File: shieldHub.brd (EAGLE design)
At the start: 70 x 70 mm, 11 parts

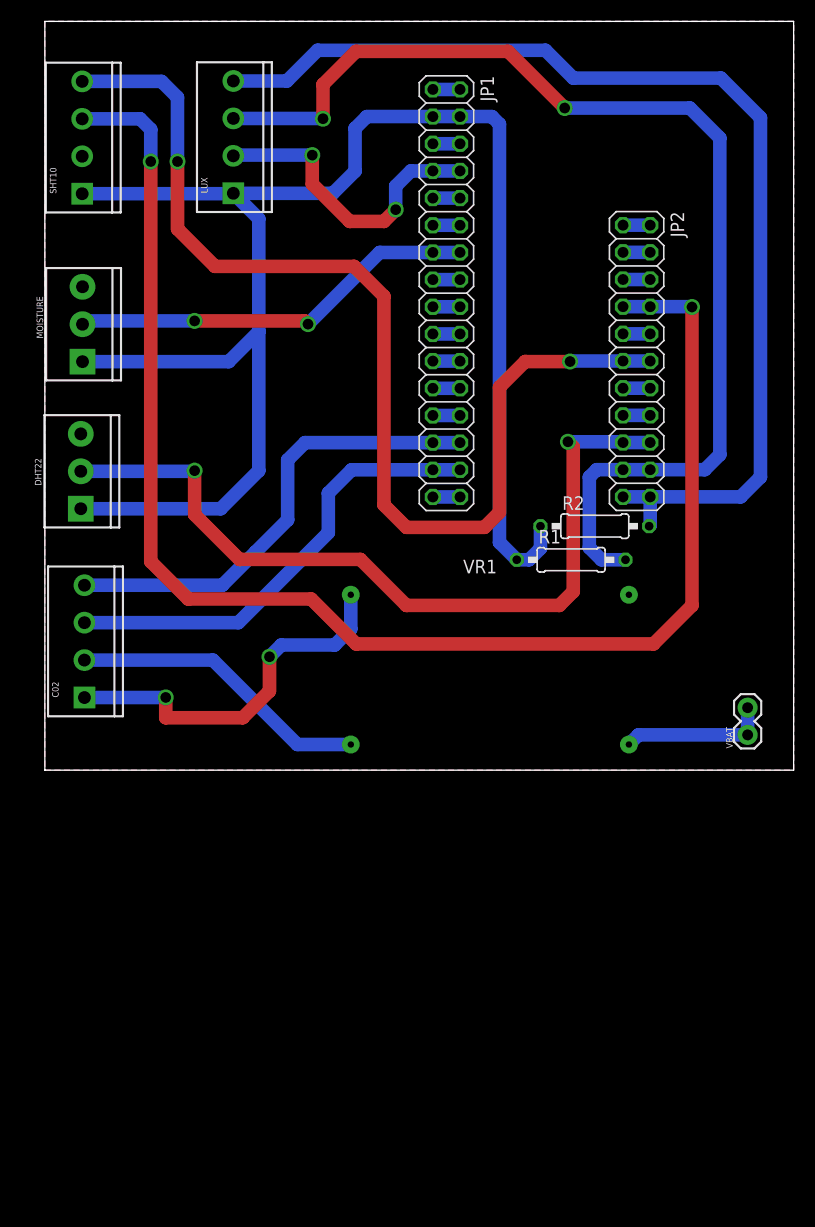
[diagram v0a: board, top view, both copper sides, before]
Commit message: Removes sensor connector pins and adds rrm69 header pin
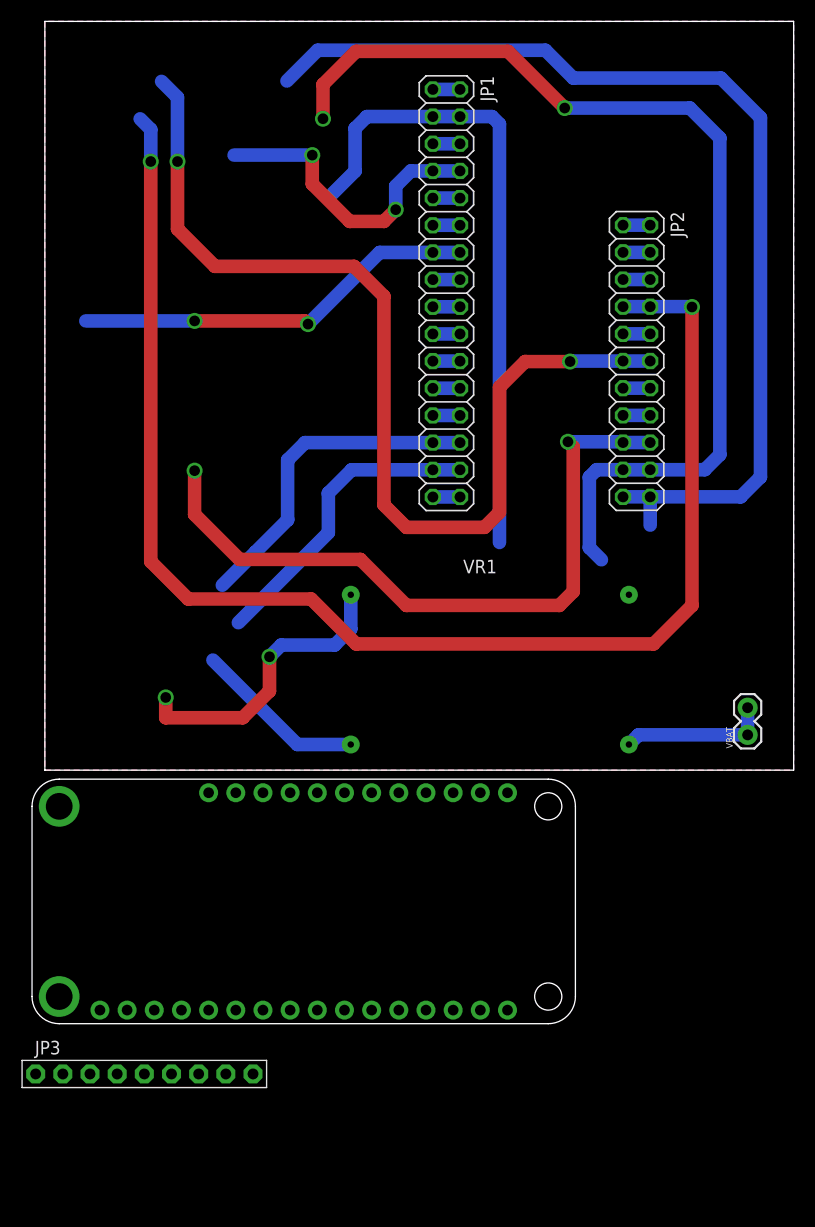
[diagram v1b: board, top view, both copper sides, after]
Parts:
- removed C02, LUX, SHT10: (no value), SparkFun-Connectors:SCREWTERMINAL-3.5MM-4
- removed DHT22, MOISTURE: (no value), SparkFun-Connectors:SCREWTERMINAL-3.5MM-3
- removed R1, R2: 10k, resistor:0207/10
- added JP3: (no value), adafruit:1X09-BIG
- added MS1: FEATHERWING, adafruit:FEATHERWING
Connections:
- net 10_SDA: no longer SHT10.4
- net 12_SCL: no longer SHT10.3
- net 3V: no longer DHT22.1, LUX.1, MOISTURE.1, R1.1, R2.1, SHT10.1
- net 5V: no longer C02.2
- net A2: no longer MOISTURE.2
- net D5: no longer DHT22.2
- net GND: now also MS1.4; no longer C02.1, DHT22.3, LUX.2, MOISTURE.3, SHT10.2
- net RX: no longer C02.4
- net SCL: no longer LUX.3, R1.2
- net SDA: no longer LUX.4, R2.2
- net TX: no longer C02.3
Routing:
- net 3V: track 153.4 -> 60.3 mm
- net TX: track 43.2 -> 28.8 mm
- net RX: track 43.9 -> 31.0 mm
- net 5V: track 28.2 -> 16.2 mm
- net SCL: track 106.4 -> 95.8 mm
- net D5: track 76.2 -> 65.6 mm
- net GND: track 63.9 -> 56.2 mm
- net 10_SDA: track 102.3 -> 94.9 mm
- net 12_SCL: track 136.9 -> 131.4 mm
- net SDA: track 103.1 -> 97.9 mm

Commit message: Adds connector pin for fan power
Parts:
- added VFAN: (no value), SparkFun-Connectors:1X02
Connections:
- removed net 5V: VR1.OUT+
- new net 12V: VFAN.1, VR1.OUT+
- net GND: now also VFAN.2
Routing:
- net 5V: track 16.2 -> 0.00 mm
- net 12V: track 0.00 -> 16.2 mm
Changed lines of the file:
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@@
 <attribute name="VALUE" x="-0.86" y="-31.575" size="1.27" layer="27"/>
+</element>
+<element name="VFAN" library="SparkFun-Connectors" package="1X02" value="" x="-0.4" y="-32.1" smashed="yes">
+<attribute name="NAME" x="-1.67" y="-30.703" size="0.6096" layer="25" font="vector" ratio="20"/>
+<attribute name="VALUE" x="-1.67" y="-34.132" size="0.6096" layer="27" font="vector" ratio="20"/>
 </element>
 </elements>
@@
 <wire x1="21" y1="7.4" x2="18.5" y2="4.9" width="1.27" layer="1"/>
 <contactref element="MS1" pad="4"/>
+<contactref element="VFAN" pad="2"/>
 <wire x1="28.6" y1="16.4" x2="32.8" y2="52.4" width="0" layer="19" extent="1-1"/>
 <wire x1="54.6" y1="16.4" x2="28.6" y2="16.4" width="0" layer="19" extent="1-1"/>
 <wire x1="12.77" y1="-22.43" x2="11.29" y2="6.79" width="0" layer="19" extent="16-16"/>
+<wire x1="2.14" y1="-32.1" x2="12.77" y2="-22.43" width="0" layer="19" extent="1-1"/>
 </signal>
 <signal name="N$1">
@@
 <wire x1="55.5" y1="3.3" x2="65.7" y2="3.3" width="1.27" layer="16"/>
 </signal>
-<signal name="5V">
+<signal name="12V">
 <contactref element="VR1" pad="OUT+"/>
 <wire x1="23.6" y1="2.4" x2="28.6" y2="2.4" width="1.27" layer="16"/>
 <wire x1="15.71" y1="10.29" x2="23.6" y2="2.4" width="1.27" layer="16"/>
+<contactref element="VFAN" pad="1"/>
+<wire x1="28.6" y1="2.4" x2="-0.4" y2="-32.1" width="0" layer="19" extent="1-1"/>
 </signal>
 <signal name="10_SDA">

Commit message: Adds connector for button
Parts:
- added BUTTON: (no value), SparkFun-Connectors:SCREWTERMINAL-3.5MM-2_LOCK
- renumbered JP3 to RFM69
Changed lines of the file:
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@@
 </element>
 <element name="MS1" library="adafruit" package="FEATHERWING" value="FEATHERWING" x="-1.2" y="-23.7" smashed="yes"/>
-<element name="JP3" library="adafruit" package="1X09-BIG" value="" x="9.3" y="-28.4" smashed="yes">
+<element name="RFM69" library="adafruit" package="1X09-BIG" value="" x="9.3" y="-28.4" smashed="yes">
 <attribute name="NAME" x="-0.9362" y="-26.5712" size="1.27" layer="25" ratio="10"/>
 <attribute name="VALUE" x="-0.86" y="-31.575" size="1.27" layer="27"/>
@@
 <attribute name="VALUE" x="-1.67" y="-34.132" size="0.6096" layer="27" font="vector" ratio="20"/>
 </element>
+<element name="BUTTON" library="SparkFun-Connectors" package="SCREWTERMINAL-3.5MM-2_LOCK" value="" x="0.1" y="-37" smashed="yes">
+<attribute name="NAME" x="-1.17" y="-34.46" size="0.6096" layer="25" font="vector" ratio="20"/>
+<attribute name="PROD_ID" value="CONN-08399" x="0.1" y="-37" size="1.778" layer="27" display="off"/>
+<attribute name="VALUE" x="-1.17" y="-35.73" size="0.6096" layer="27" font="vector" ratio="20"/>
+</element>
 </elements>

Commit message: Connects rfm69 to boron
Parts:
- removed JP2: (no value), pinhead:2X11
- removed MS1: FEATHERWING, adafruit:FEATHERWING
- added JP3: (no value), pinhead:2X12
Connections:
- removed net 10_SDA: JP2.11, JP2.12
- removed net 12_SCL: JP2.7, JP2.8
- removed net A2: JP1.13, JP1.14
- removed net D5: JP2.17, JP2.18
- removed net N$17: JP2.1, JP2.2
- removed net N$18: JP2.3, JP2.4
- removed net SCL: JP2.19, JP2.20
- removed net SDA: JP2.21, JP2.22
- new net N$14: JP3.21, JP3.22
- new net N$2: BUTTON.2
- new net N$25: JP3.1, JP3.2
- new net N$4: BUTTON.1
- new net N$7: JP3.23, JP3.24
- new net RFM69_CS: JP1.13, JP1.14, RFM69.8
- new net RFM69_G0: JP3.7, JP3.8, RFM69.4
- new net RFM69_MISO: JP3.15, JP3.16, RFM69.6
- new net RFM69_MOSI: JP3.17, JP3.18, RFM69.7
- new net RFM69_RST: JP3.11, JP3.12, RFM69.9
- new net RFM69_SCK: JP3.19, JP3.20, RFM69.5
- net 3V: now also RFM69.1
- net GND: now also RFM69.2; no longer MS1.4
- net N$19: now also JP3.13, JP3.14; no longer JP2.5, JP2.6
- net N$21: now also JP3.10, JP3.9; no longer JP2.10, JP2.9
- net N$23: now also JP3.5, JP3.6; no longer JP2.13, JP2.14
- net N$24: now also JP3.3, JP3.4; no longer JP2.15, JP2.16
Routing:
- net 12_SCL: track 131.4 -> 0.00 mm, vias 2 -> 0
- net SDA: track 97.9 -> 0.00 mm
- net SCL: track 95.8 -> 0.00 mm, vias 2 -> 0
- net 10_SDA: track 94.9 -> 0.00 mm, vias 2 -> 0
- net D5: track 65.6 -> 0.00 mm, vias 2 -> 0
- net RFM69_CS: track 0.00 -> 37.9 mm, vias 0 -> 2
- net A2: track 37.9 -> 0.00 mm, vias 2 -> 0
- net N$24: track 2.54 -> 0.00 mm
- net N$23: track 2.54 -> 0.00 mm
- net N$21: track 2.54 -> 0.00 mm
- net N$19: track 2.54 -> 0.00 mm
- net N$18: track 2.54 -> 0.00 mm
- net N$17: track 2.54 -> 0.00 mm

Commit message: Connects button to boron
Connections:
- removed net N$2: BUTTON.2
- removed net N$4: BUTTON.1
- removed net N$9: JP1.17, JP1.18
- new net IRR_BUTT: BUTTON.1, JP1.17, JP1.18
- net GND: now also BUTTON.2
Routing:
- net N$9: track 2.54 -> 0.00 mm
- net IRR_BUTT: track 0.00 -> 2.54 mm
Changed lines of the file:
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@@
 <contactref element="VFAN" pad="2"/>
 <contactref element="RFM69" pad="2"/>
+<contactref element="BUTTON" pad="2"/>
 <wire x1="28.6" y1="16.4" x2="32.8" y2="52.4" width="0" layer="19" extent="1-1"/>
 <wire x1="54.6" y1="16.4" x2="28.6" y2="16.4" width="0" layer="19" extent="1-1"/>
 <wire x1="1.68" y1="-28.4" x2="11.29" y2="6.79" width="0" layer="19" extent="16-16"/>
 <wire x1="2.14" y1="-32.1" x2="1.68" y2="-28.4" width="0" layer="19" extent="1-1"/>
+<wire x1="3.7778" y1="-37" x2="2.14" y2="-32.1" width="0" layer="19" extent="1-1"/>
 </signal>
 <signal name="N$1">
@@
 <wire x1="36.273" y1="45.861" x2="38.813" y2="45.861" width="1.27" layer="16"/>
 </signal>
-<signal name="N$9">
+<signal name="IRR_BUTT">
 <contactref element="JP1" pad="17"/>
 <contactref element="JP1" pad="18"/>
 <wire x1="36.273" y1="43.321" x2="38.813" y2="43.321" width="1.27" layer="16"/>
+<contactref element="BUTTON" pad="1"/>
+<wire x1="-0.0778" y1="-37" x2="36.273" y2="43.321" width="0" layer="19" extent="1-1"/>
 </signal>
 <signal name="N$10">
@@
 <wire x1="6.76" y1="-28.4" x2="54.13" y2="45.85" width="0" layer="19" extent="1-1"/>
 </signal>
-<signal name="N$2">
-<contactref element="BUTTON" pad="2"/>
-</signal>
-<signal name="N$4">
-<contactref element="BUTTON" pad="1"/>
-</signal>
 <signal name="N$7">

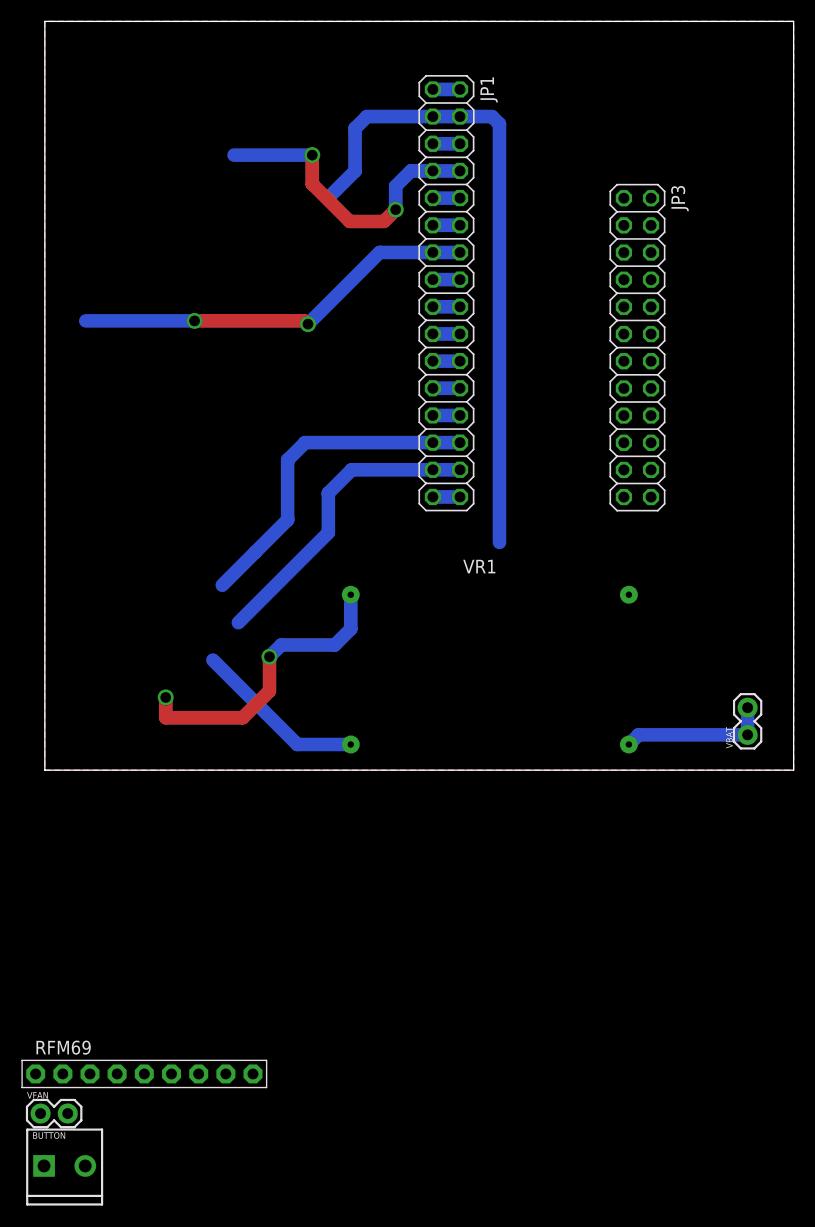
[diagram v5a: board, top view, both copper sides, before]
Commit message: Completes routing of brd file
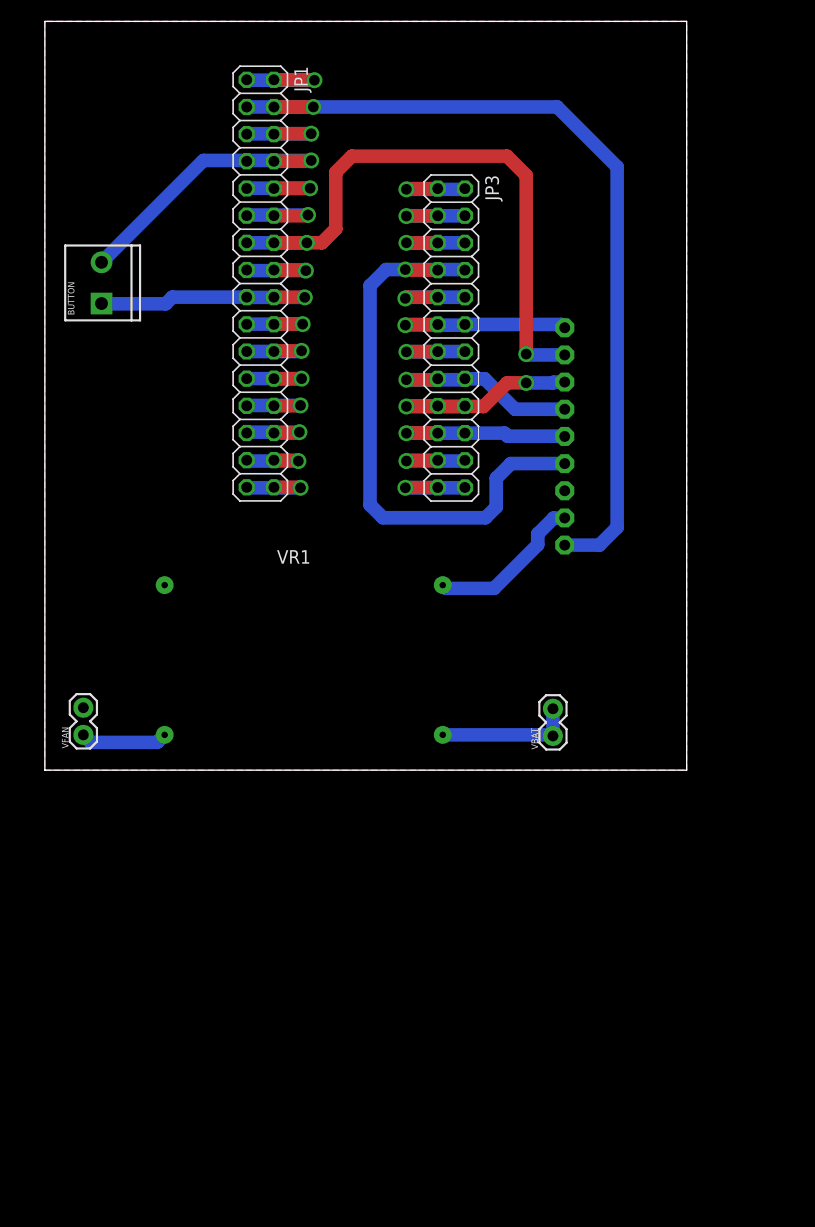
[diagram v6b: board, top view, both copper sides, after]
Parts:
- moved BUTTON 81.0 mm to (5.30, 43.8), turned to 90 degrees
- moved RFM69 71.4 mm to (48.6, 31.2), flipped to the bottom, turned to 90 degrees
- moved VFAN 35.6 mm to (3.60, 3.30), turned to 90 degrees
- moved VBAT 18.2 mm to (47.5, 3.20)
- moved VR1 17.4 mm to (11.2, 17.3)
- moved JP1 17.4 mm to (20.1, 45.5)
- moved JP3 17.4 mm to (38.0, 40.4)
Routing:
- net RFM69_G0: track 0.00 -> 55.4 mm, vias 0 -> 1
- net RFM69_MOSI: track 0.00 -> 24.2 mm, vias 0 -> 2
- net RX: track 31.0 -> 7.38 mm, vias 0 -> 1
- net TX: track 28.8 -> 7.18 mm, vias 0 -> 1
- net 3V: track 60.3 -> 79.9 mm, vias 0 -> 1
- net IRR_BUTT: track 2.54 -> 22.2 mm, vias 0 -> 1
- net RFM69_MISO: track 0.00 -> 19.0 mm, vias 0 -> 1
- net RFM69_CS: track 37.9 -> 56.8 mm
- net RFM69_RST: track 0.00 -> 18.1 mm, vias 0 -> 1
- net RFM69_SCK: track 0.00 -> 17.9 mm, vias 0 -> 1
- net GND: track 56.2 -> 42.0 mm, vias 4 -> 1
- net N$21: track 0.00 -> 8.69 mm, vias 0 -> 1
- net N$7: track 0.00 -> 8.62 mm, vias 0 -> 1
- net N$25: track 0.00 -> 8.46 mm, vias 0 -> 1
- net N$14: track 0.00 -> 8.46 mm, vias 0 -> 1
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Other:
- board size 70 x 70 mm -> 60 x 70 mm

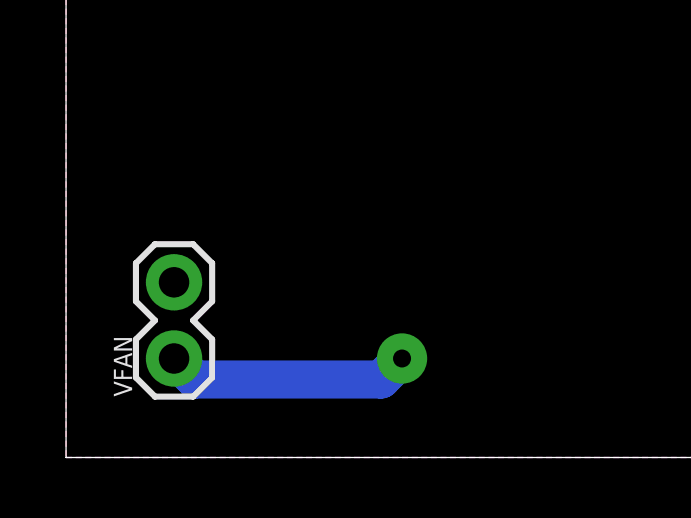
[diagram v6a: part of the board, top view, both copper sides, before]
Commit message: Replaces fan power header pin with a connector pin
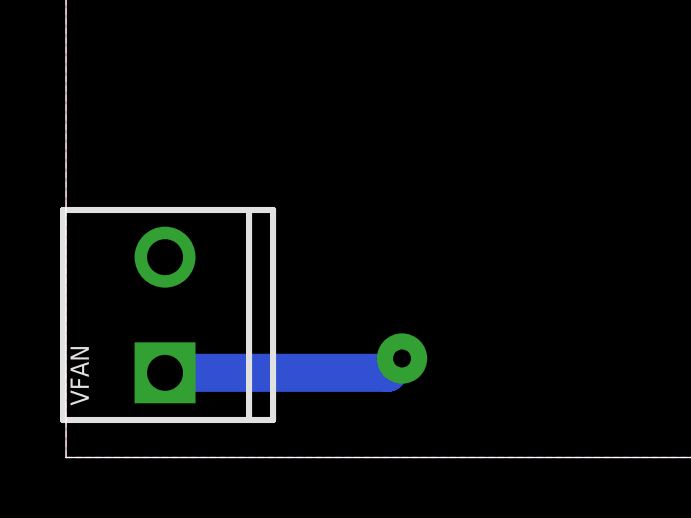
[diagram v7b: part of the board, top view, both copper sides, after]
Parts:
- VFAN: device SparkFun-Connectors:1X02 -> SparkFun-Connectors:SCREWTERMINAL-3.5MM-2_LOCK
- moved VFAN 0.42 mm to (3.30, 3.00)
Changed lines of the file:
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@@
 <setting verticaltext="up"/>
 </settings>
-<grid distance="1" unitdist="mm" unit="mm" style="dots" multiple="1" display="yes" altdistance="5" altunitdist="mil" altunit="mm"/>
+<grid distance="0.1" unitdist="mm" unit="mm" style="dots" multiple="1" display="yes" altdistance="5" altunitdist="mil" altunit="mm"/>
 <layers>
 <layer number="1" name="Top" color="4" fill="1" visible="yes" active="yes"/>
@@
 <attribute name="VALUE" x="45.425" y="21.04" size="1.27" layer="28" rot="MR90"/>
 </element>
-<element name="VFAN" library="SparkFun-Connectors" package="1X02" value="" x="3.6" y="3.3" smashed="yes" rot="R90">
-<attribute name="NAME" x="2.203" y="2.03" size="0.6096" layer="25" font="vector" ratio="20" rot="R90"/>
-<attribute name="VALUE" x="5.632" y="2.03" size="0.6096" layer="27" font="vector" ratio="20" rot="R90"/>
-</element>
 <element name="BUTTON" library="SparkFun-Connectors" package="SCREWTERMINAL-3.5MM-2_LOCK" value="" x="5.3" y="43.8" smashed="yes" rot="R90">
 <attribute name="NAME" x="2.76" y="42.53" size="0.6096" layer="25" font="vector" ratio="20" rot="R90"/>
@@
 <attribute name="POPULARITY" value="3" x="38" y="40.4" locked="yes" size="1.778" layer="27" rot="R270" display="off"/>
 <attribute name="VALUE" x="33.555" y="55.64" locked="yes" size="1.27" layer="27" rot="R270"/>
+</element>
+<element name="VFAN" library="SparkFun-Connectors" package="SCREWTERMINAL-3.5MM-2_LOCK" value="" x="3.3" y="3" smashed="yes" rot="R90">
+<attribute name="NAME" x="0.76" y="1.73" size="0.6096" layer="25" font="vector" ratio="20" rot="R90"/>
+<attribute name="PROD_ID" value="CONN-08399" x="3.3" y="3" size="1.778" layer="27" rot="R90" display="off"/>
+<attribute name="VALUE" x="2.03" y="1.73" size="0.6096" layer="27" font="vector" ratio="20" rot="R90"/>
 </element>
 </elements>
@@
 <vertex x="0" y="70"/>
 </polygon>
-<contactref element="VFAN" pad="2"/>
 <contactref element="RFM69" pad="2"/>
 <contactref element="BUTTON" pad="2"/>
@@
 <wire x1="42" y1="17" x2="37.5" y2="17" width="1.27" layer="16"/>
 <wire x1="37.5" y1="17" x2="37.2" y2="17.3" width="1.27" layer="16"/>
+<contactref element="VFAN" pad="2"/>
 </signal>
 <signal name="N$1">
@@
 <contactref element="VR1" pad="OUT+"/>
 <contactref element="VFAN" pad="1"/>
-<wire x1="3.6" y1="3.3" x2="4.3" y2="2.6" width="1.27" layer="16"/>
-<wire x1="10.5" y1="2.6" x2="11.2" y2="3.3" width="1.27" layer="16"/>
-<wire x1="4.3" y1="2.6" x2="10.5" y2="2.6" width="1.27" layer="16"/>
+<wire x1="3.3" y1="2.8222" x2="10.7222" y2="2.8222" width="1.27" layer="16"/>
+<wire x1="10.7222" y1="2.8222" x2="11.2" y2="3.3" width="1.27" layer="16"/>
 </signal>
 <signal name="RFM69_RST">
